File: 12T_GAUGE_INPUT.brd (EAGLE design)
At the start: 71.1 x 63.2 mm, 111 parts, among them J1 MICRO-SD_CARD_SOCKET, P1_WP_PULLUP 10k, P2_WP_PULLUP 10k, P3_WP_PULLUP 10k

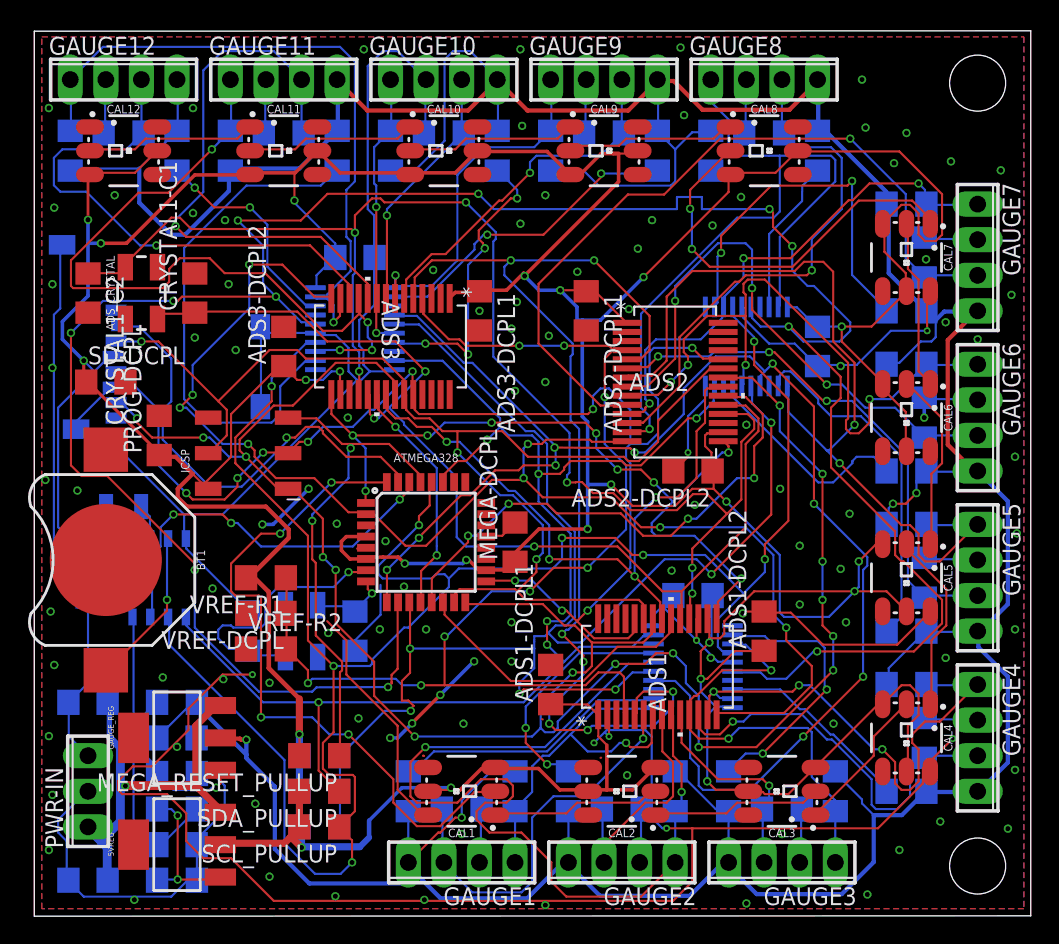
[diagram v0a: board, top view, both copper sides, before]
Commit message: ADD MORE GROUND PLANE
update: board wasn't finished
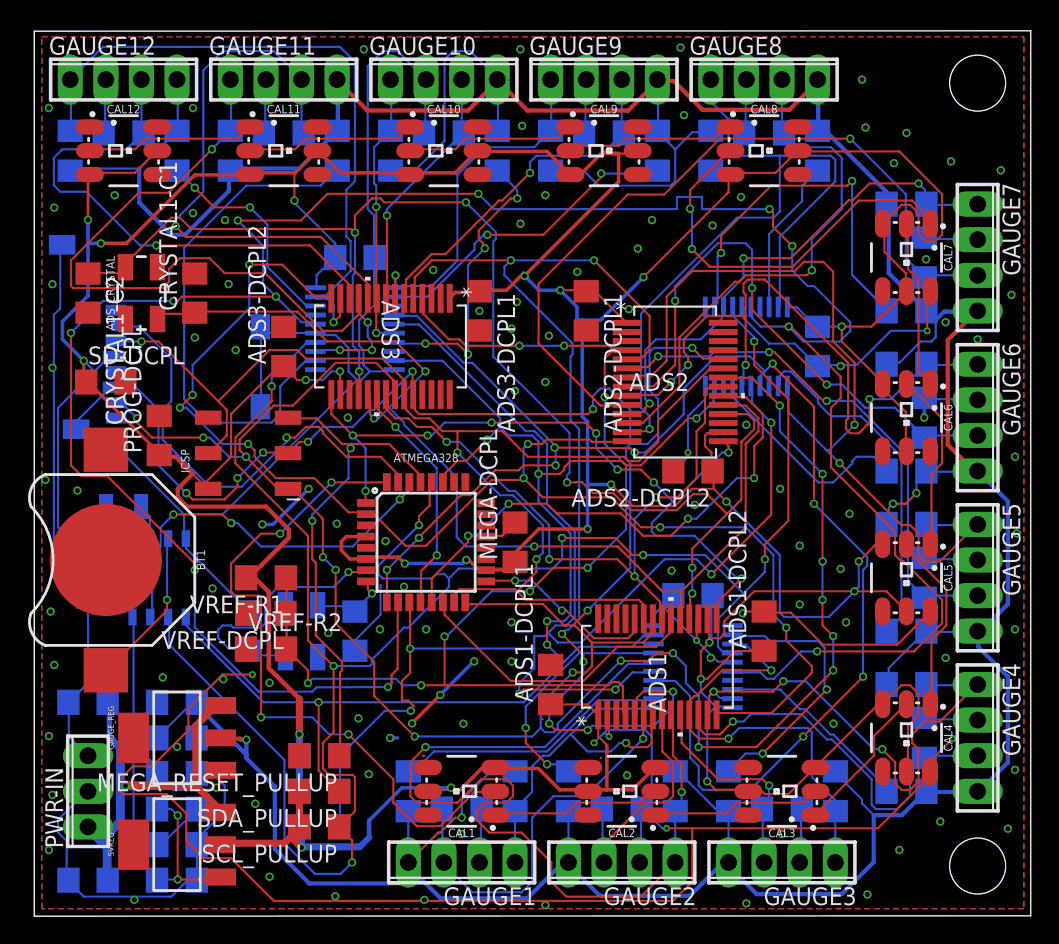
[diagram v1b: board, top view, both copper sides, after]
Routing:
- net GND: track 398.1 -> 379.1 mm, vias 111 -> 112
- net VREF: track 85.5 -> 84.4 mm
- net ADS_SYNC: track 98.1 -> 97.6 mm
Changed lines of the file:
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@@
 <wire x1="63.7032" y1="16.4592" x2="63.652" y2="16.51" width="0.1524" layer="16"/>
 <wire x1="67.2084" y1="16.4592" x2="67.31" y2="16.51" width="0.1524" layer="16"/>
-<wire x1="54.102" y1="16.002" x2="48.4632" y2="16.002" width="0.1524" layer="1"/>
-<wire x1="54.5592" y1="16.4592" x2="54.102" y2="16.002" width="0.1524" layer="1"/>
-<wire x1="55.3212" y1="16.4592" x2="54.5592" y2="16.4592" width="0.1524" layer="16"/>
-<wire x1="59.8932" y1="11.8872" x2="55.3212" y2="16.4592" width="0.1524" layer="16"/>
+<wire x1="52.705" y1="16.002" x2="48.4632" y2="16.002" width="0.1524" layer="1"/>
+<wire x1="53.4416" y1="16.7386" x2="52.705" y2="16.002" width="0.1524" layer="1"/>
+<wire x1="55.0418" y1="16.7386" x2="53.4416" y2="16.7386" width="0.1524" layer="16"/>
+<wire x1="59.8932" y1="11.8872" x2="55.0418" y2="16.7386" width="0.1524" layer="16"/>
 <wire x1="60.5028" y1="11.8872" x2="59.8932" y2="11.8872" width="0.1524" layer="16"/>
 <wire x1="61.4172" y1="10.9728" x2="60.5028" y2="11.8872" width="0.1524" layer="1"/>
@@
 <wire x1="67.2084" y1="16.4592" x2="67.31" y2="16.51" width="0.1524" layer="1"/>
 <via x="48.4632" y="16.002" extent="1-16" drill="0.35"/>
-<via x="54.5592" y="16.4592" extent="1-16" drill="0.35"/>
+<via x="53.4416" y="16.7386" extent="1-16" drill="0.35"/>
 <via x="60.5028" y="11.8872" extent="1-16" drill="0.35"/>
 </signal>
@@
 <wire x1="51.816" y1="17.3736" x2="49.8348" y2="17.3736" width="0.1524" layer="16"/>
 <wire x1="52.2732" y1="16.9164" x2="51.816" y2="17.3736" width="0.1524" layer="16"/>
-<wire x1="53.6448" y1="16.9164" x2="52.2732" y2="16.9164" width="0.1524" layer="16"/>
-<wire x1="55.6006" y1="18.8722" x2="53.6448" y2="16.9164" width="0.1524" layer="16"/>
+<wire x1="52.7558" y1="16.9164" x2="52.2732" y2="16.9164" width="0.1524" layer="16"/>
+<wire x1="54.7116" y1="18.8722" x2="52.7558" y2="16.9164" width="0.1524" layer="16"/>
 <wire x1="62.7634" y1="18.8722" x2="55.8546" y2="18.8722" width="0.1524" layer="1"/>
 <wire x1="64.77" y1="20.8788" x2="62.7634" y2="18.8722" width="0.1524" layer="1"/>
@@
 <wire x1="25.4762" y1="16.5862" x2="25.4762" y2="16.6878" width="0.1524" layer="1"/>
 <wire x1="25.2222" y1="16.3322" x2="25.4762" y2="16.5862" width="0.1524" layer="1"/>
-<wire x1="55.8546" y1="18.8722" x2="55.6006" y2="18.8722" width="0.1524" layer="16"/>
+<wire x1="55.8546" y1="18.8722" x2="54.7116" y2="18.8722" width="0.1524" layer="16"/>
 <wire x1="52.451" y1="50.4444" x2="52.705" y2="50.1904" width="0.1524" layer="1"/>
 <wire x1="53.8226" y1="42.0624" x2="53.9496" y2="42.0624" width="0.1524" layer="1"/>
@@
 <wire x1="24.6888" y1="21.4884" x2="22.86" y2="19.6596" width="0.1524" layer="16"/>
 <wire x1="24.6888" y1="23.622" x2="24.6888" y2="21.4884" width="0.1524" layer="16"/>
-<wire x1="23.622" y1="26.2128" x2="23.0124" y2="26.2128" width="0.1524" layer="1"/>
 <wire x1="23.622" y1="26.2128" x2="23.6474" y2="26.27" width="0.1524" layer="1"/>
-<wire x1="27.5844" y1="7.3152" x2="28.0416" y2="7.3152" width="0.1524" layer="1"/>
-<wire x1="25.908" y1="8.9916" x2="27.5844" y2="7.3152" width="0.1524" layer="1"/>
-<wire x1="25.908" y1="13.5636" x2="25.908" y2="8.9916" width="0.1524" layer="1"/>
-<wire x1="22.2504" y1="17.2212" x2="25.908" y2="13.5636" width="0.1524" layer="1"/>
-<wire x1="22.2504" y1="19.6596" x2="22.2504" y2="17.2212" width="0.1524" layer="1"/>
-<wire x1="20.8788" y1="21.0312" x2="22.2504" y2="19.6596" width="0.1524" layer="1"/>
 <wire x1="28.0416" y1="7.3152" x2="28.08" y2="7.19" width="0.1524" layer="1"/>
 <wire x1="11.5824" y1="2.5908" x2="11.5824" y2="5.0292" width="0.1524" layer="16"/>
@@
 <wire x1="26.94359375" y1="13.75819375" x2="26.94359375" y2="13.73559375" width="0.254" layer="1"/>
 <via x="26.94359375" y="13.73559375" extent="1-16" drill="0.35"/>
-<wire x1="26.94359375" y1="13.73559375" x2="25.908" y2="12.7" width="0.254" layer="16"/>
 <wire x1="25.908" y1="12.7" x2="25.3774" y2="12.7" width="0.254" layer="16"/>
 <via x="25.3774" y="12.7" extent="1-16" drill="0.35"/>
@@
 <via x="26.3652" y="23.495" extent="1-16" drill="0.35"/>
 <via x="25.0444" y="26.7462" extent="1-16" drill="0.35"/>
-<wire x1="23.6474" y1="26.27" x2="25.0444" y2="26.7462" width="0" layer="19" extent="1-1"/>
+<via x="23.8506" y="10.1092" extent="1-16" drill="0.35"/>
+<wire x1="30.48" y1="5.842" x2="28.08" y2="7.19" width="0" layer="19" extent="1-1"/>
 </signal>
 <signal name="B2+">
@@
 <wire x1="67.31" y1="34.29" x2="63.5508" y2="34.29" width="0.1524" layer="16"/>
 <wire x1="63.5508" y1="34.29" x2="63.5" y2="34.138" width="0.1524" layer="16"/>
-<wire x1="43.7388" y1="37.7952" x2="42.3672" y2="37.7952" width="0.1524" layer="1"/>
-<wire x1="45.72" y1="39.7764" x2="43.7388" y2="37.7952" width="0.1524" layer="1"/>
-<wire x1="45.72" y1="43.8912" x2="45.72" y2="39.7764" width="0.1524" layer="1"/>
+<wire x1="44.1706" y1="37.7952" x2="42.3672" y2="37.7952" width="0.1524" layer="1"/>
+<wire x1="45.72" y1="39.3446" x2="44.1706" y2="37.7952" width="0.1524" layer="1"/>
+<wire x1="45.72" y1="43.8912" x2="45.72" y2="39.3446" width="0.1524" layer="1"/>
 <wire x1="45.72" y1="44.958" x2="45.72" y2="43.8912" width="0.1524" layer="16"/>
 <wire x1="48.768" y1="48.006" x2="45.72" y2="44.958" width="0.1524" layer="16"/>
@@
 <wire x1="17.9832" y1="21.4884" x2="17.9832" y2="19.05" width="0.1524" layer="1"/>
 <wire x1="17.9832" y1="21.4884" x2="17.91" y2="21.59" width="0.1524" layer="1"/>
-<wire x1="42.0624" y1="17.0688" x2="42.0624" y2="14.478" width="0.1524" layer="1"/>
-<wire x1="41.7576" y1="17.3736" x2="42.0624" y2="17.0688" width="0.1524" layer="1"/>
-<wire x1="40.2336" y1="17.3736" x2="41.7576" y2="17.3736" width="0.1524" layer="1"/>
-<wire x1="39.3192" y1="16.4592" x2="40.2336" y2="17.3736" width="0.1524" layer="1"/>
+<wire x1="41.2242" y1="16.6878" x2="41.6814" y2="16.6878" width="0.1524" layer="1"/>
+<wire x1="41.6814" y1="16.6878" x2="41.9862" y2="16.383" width="0.1524" layer="1"/>
+<wire x1="41.9862" y1="16.383" x2="41.9862" y2="14.56394375" width="0.1524" layer="1"/>
+<wire x1="40.9956" y1="16.4592" x2="41.2242" y2="16.6878" width="0.1524" layer="1"/>
 <wire x1="27.5844" y1="16.4592" x2="29.2608" y2="16.4592" width="0.1524" layer="1"/>
-<wire x1="29.5148" y1="16.4592" x2="39.3192" y2="16.4592" width="0.1524" layer="1"/>
+<wire x1="29.5148" y1="16.4592" x2="40.9956" y2="16.4592" width="0.1524" layer="1"/>
 <wire x1="26.2382" y1="16.4592" x2="27.5844" y2="16.4592" width="0.1524" layer="16"/>
 <wire x1="25.781" y1="16.9164" x2="26.2382" y2="16.4592" width="0.1524" layer="16"/>
@@
 <wire x1="19.5072" y1="17.526" x2="19.5072" y2="16.6116" width="0.1524" layer="1"/>
 <wire x1="17.9832" y1="19.05" x2="19.5072" y2="17.526" width="0.1524" layer="1"/>
-<wire x1="42.0624" y1="14.478" x2="42.175" y2="14.351" width="0.1524" layer="1"/>
+<wire x1="41.9862" y1="14.56394375" x2="42.175" y2="14.351" width="0.1524" layer="1"/>
 <wire x1="17.9832" y1="19.05" x2="17.932" y2="19.05" width="0.1524" layer="1"/>
 <wire x1="40.6908" y1="39.7764" x2="41.3004" y2="40.386" width="0.1524" layer="1"/>
@@
 <wire x1="45.5676" y1="18.7452" x2="46.482" y2="17.8308" width="0.1524" layer="16"/>
 <wire x1="44.3484" y1="18.7452" x2="45.5676" y2="18.7452" width="0.1524" layer="1"/>
-<wire x1="43.5864" y1="17.9832" x2="44.3484" y2="18.7452" width="0.1524" layer="1"/>
-<wire x1="41.4528" y1="17.9832" x2="43.5864" y2="17.9832" width="0.1524" layer="1"/>
-<wire x1="37.338" y1="13.8684" x2="41.4528" y2="17.9832" width="0.1524" layer="16"/>
-<wire x1="37.338" y1="13.4112" x2="37.338" y2="13.8684" width="0.1524" layer="16"/>
+<wire x1="43.7896" y1="18.1864" x2="44.3484" y2="18.7452" width="0.1524" layer="1"/>
+<wire x1="41.8592" y1="18.1864" x2="43.7896" y2="18.1864" width="0.1524" layer="1"/>
+<wire x1="37.338" y1="13.716" x2="41.8338" y2="18.2118" width="0.1524" layer="16"/>
+<wire x1="37.338" y1="13.4112" x2="37.338" y2="13.716" width="0.1524" layer="16"/>
 <wire x1="37.0332" y1="13.1064" x2="37.338" y2="13.4112" width="0.1524" layer="16"/>
 <wire x1="36.4236" y1="13.1064" x2="37.0332" y2="13.1064" width="0.1524" layer="16"/>
@@
 <via x="47.3964" y="12.0396" extent="1-16" drill="0.35"/>
 <via x="45.5676" y="18.7452" extent="1-16" drill="0.35"/>
-<via x="41.4528" y="17.9832" extent="1-16" drill="0.35"/>
+<via x="41.8338" y="18.2118" extent="1-16" drill="0.35"/>
 <via x="38.4048" y="17.3736" extent="1-16" drill="0.35"/>
 <via x="20.574" y="25.6032" extent="1-16" drill="0.35"/>
 <via x="21.4884" y="24.6888" extent="1-16" drill="0.35"/>
 <via x="27.1272" y="12.8016" extent="1-16" drill="0.35"/>
+<wire x1="41.8592" y1="18.1864" x2="41.8338" y2="18.2118" width="0.1524" layer="1"/>
 </signal>
 <signal name="ADS_DRDY">
@@
 <wire x1="21.0312" y1="44.196" x2="21.175003125" y2="44.069" width="0.1524" layer="1"/>
 <wire x1="23.622" y1="28.8036" x2="23.6474" y2="28.67" width="0.1524" layer="1"/>
-<wire x1="53.4924" y1="14.478" x2="48.768" y2="14.478" width="0.1524" layer="1"/>
-<wire x1="55.4736" y1="16.4592" x2="53.4924" y2="14.478" width="0.1524" layer="1"/>
-<wire x1="55.4736" y1="17.8308" x2="55.4736" y2="16.4592" width="0.1524" layer="1"/>
+<wire x1="52.6034" y1="14.478" x2="48.768" y2="14.478" width="0.1524" layer="1"/>
+<wire x1="55.4736" y1="17.3482" x2="52.6034" y2="14.478" width="0.1524" layer="1"/>
+<wire x1="55.4736" y1="17.8308" x2="55.4736" y2="17.3482" width="0.1524" layer="1"/>
 <wire x1="53.6448" y1="19.6596" x2="55.4736" y2="17.8308" width="0.1524" layer="1"/>
 <wire x1="53.6448" y1="20.574" x2="53.6448" y2="19.6596" width="0.1524" layer="1"/>
@@
 <mfgpreviewcolor name="substratecolor" color="0xFF786E46"/>
 </mfgpreviewcolors>
+<errors>
+</errors>
 </board>
 </drawing>

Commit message: More ground plane + silkscreen readability
Still not done yet...
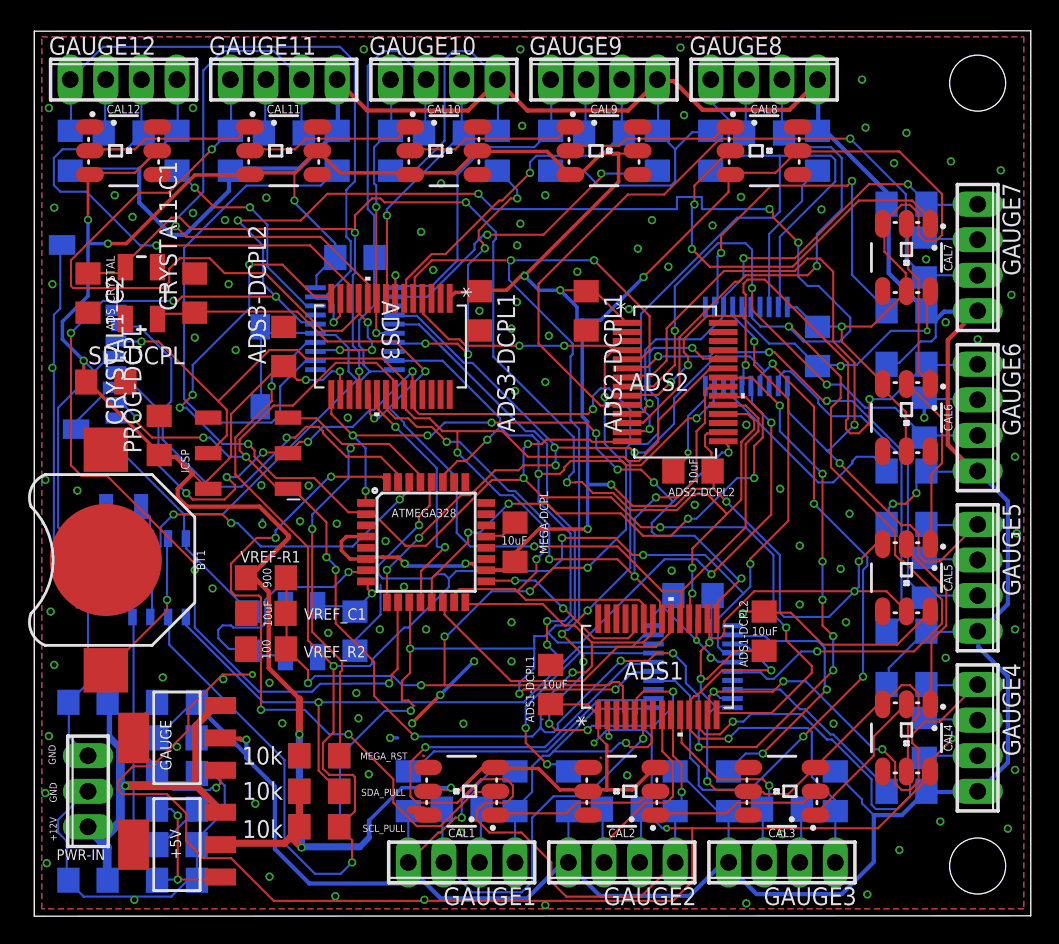
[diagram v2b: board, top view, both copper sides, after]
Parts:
- ATMEGA328: value ATMEGA328P_TQFP -> (none)
- CAL1, CAL10, CAL11, CAL12, CAL2, CAL3, CAL4, CAL5, CAL6, CAL7, CAL8, CAL9: value WS2812 -> (none)
- renumbered 5VREG to +5V, GAUGE_REG to GAUGE, MEGA_RESET_PULLUP to MEGA_RST, SCL_PULLUP to SCL_PULL, SDA_PULLUP to SDA_PULL, VREF-DCPL to VREF_C1, VREF-R2 to VREF_R2
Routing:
- net GND: track 379.1 -> 376.5 mm, vias 112 -> 123
- net B5-_P2W0: track 60.9 -> 59.8 mm
- net SCK: track 96.1 -> 97.1 mm
- net ADS3_CS: track 17.1 -> 17.9 mm
- net B1-_P1W0: track 26.6 -> 27.3 mm
- net B7-_P2W2: track 37.4 -> 36.9 mm
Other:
- board text added: "+12V"
- board text added: "GND"

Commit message: Finished silkscreen cleanup
Looks readable now, still need to add WURACING logo
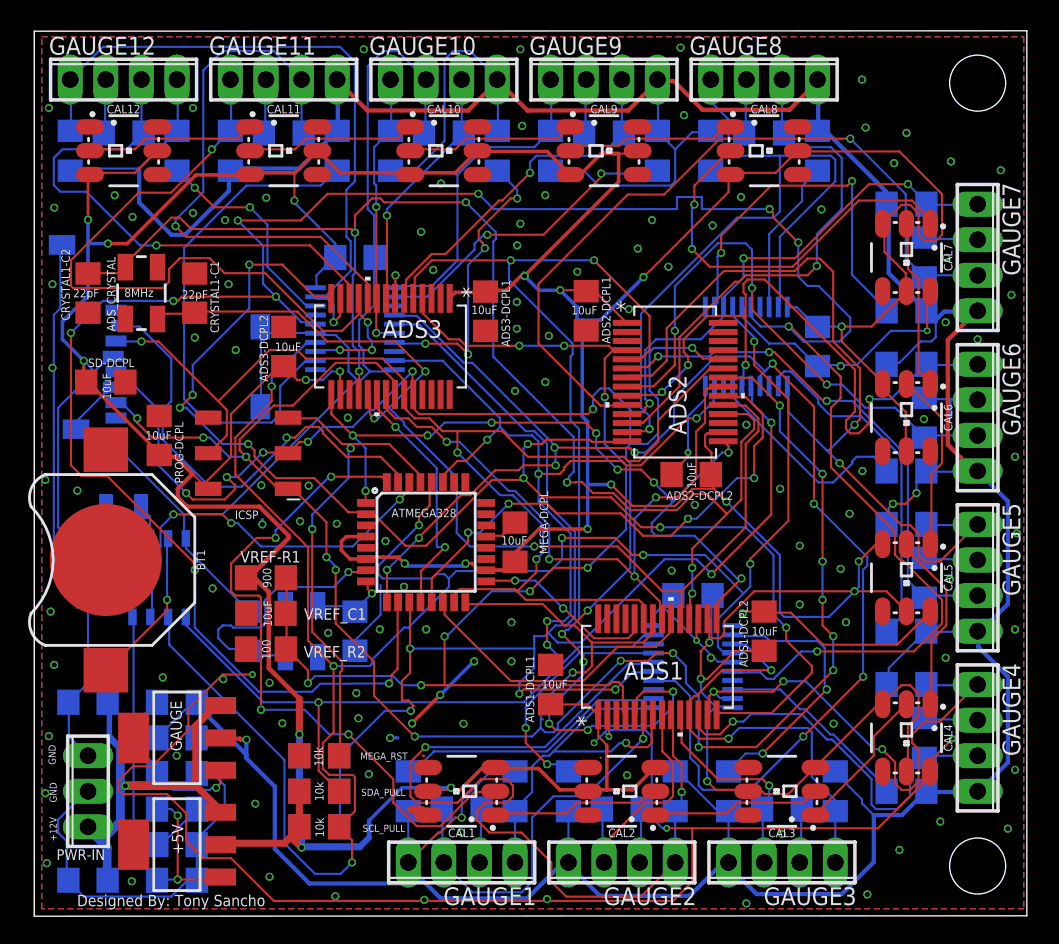
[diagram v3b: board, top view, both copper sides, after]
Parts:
- moved ADS3-DCPL1 0.43 mm to (32.2, 43.2)
- moved ADS2-DCPL2 0.28 mm to (46.9, 31.5)
- renumbered J1 to SD_SLOT, P1_WP_PULLUP to P1_WP, P2_WP_PULLUP to P2_WP, P3_WP_PULLUP to P3_WP, PWR-DCPL-AGND to PWR-DCPL1, PWR-DCPL-GND to PWR-DCPL2
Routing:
- net GND: track 376.5 -> 376.8 mm, vias 123 -> 124
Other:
- board size 71.1 x 63.2 mm -> 70.8 x 63.2 mm
- board text added: "Designed By: Tony Sancho"

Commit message: MOAR GROUND PLANE
added more ground plane area
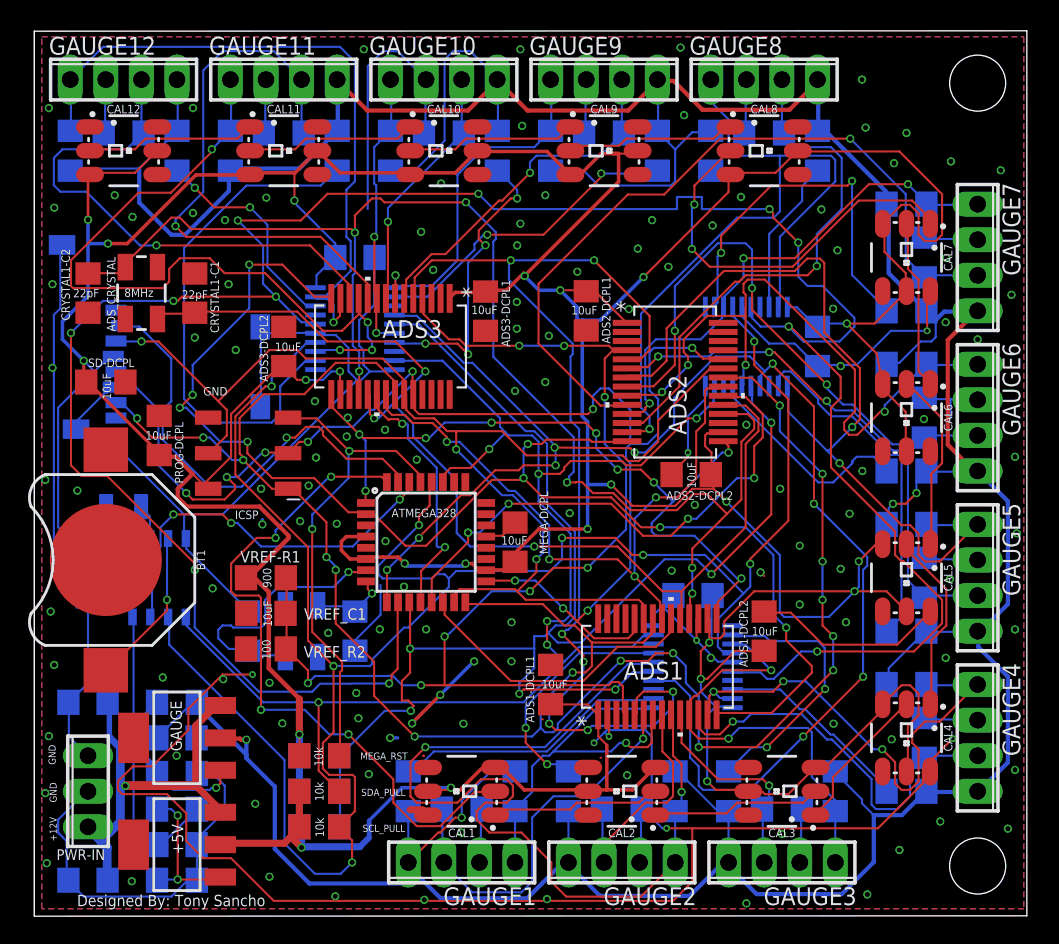
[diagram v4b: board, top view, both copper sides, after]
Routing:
- net GND: track 376.8 -> 372.1 mm, vias 124 -> 133
- net MISO: track 143.0 -> 144.0 mm
- net ADS3_CS: track 17.9 -> 18.6 mm
- net B6+: track 40.9 -> 41.5 mm
- net RESET: track 36.0 -> 35.5 mm
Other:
- board text added: "C:/Users/Frightmare/Documents/eagle/projects/FSAE/Sensorpalooza/WashU Racing Logo.bmp"
